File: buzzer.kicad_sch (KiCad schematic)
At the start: 3 parts, among them Q1 BC817

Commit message: Initial component placement
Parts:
- BZ1: footprint (none) -> Buzzer_Beeper:Buzzer_TDK_PS1240P02BT_D12.2mm_H6.5mm
- R11: footprint (none) -> Resistor_SMD:R_0805_2012Metric_Pad1.20x1.40mm_HandSolder
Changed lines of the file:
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@@
 			)
 		)
-		(property "Footprint" ""
+		(property "Footprint" "Resistor_SMD:R_0805_2012Metric_Pad1.20x1.40mm_HandSolder"
 			(at 132.08 103.378 90)
 			(effects
@@
 			)
 		)
-		(property "Footprint" ""
+		(property "Footprint" "Buzzer_Beeper:Buzzer_TDK_PS1240P02BT_D12.2mm_H6.5mm"
 			(at 147.955 90.17 90)
 			(effects

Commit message: Initial layout
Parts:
- added R33: R, Resistor_SMD:R_0805_2012Metric_Pad1.20x1.40mm_HandSolder, symbol Device:R
- BZ1: value Buzzer -> PKMCS0909E48H0-R1; footprint Buzzer_Beeper:Buzzer_TDK_PS1240P02BT_D12.2mm_H6.5mm -> Buzzer_Beeper:Buzzer_Murata_PKLCS1212E
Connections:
- net VCC: now also R33.2
- net at BZ1.2 (-), Q1.3 (C): now also R33.1
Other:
- moved on the sheet: BZ1
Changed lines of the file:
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@@
 	(generator_version "8.0")
 	(paper "A4")
+	(junction
+		(at 144.78 95.25)
+		(diameter 0)
+		(color 0 0 0 0)
+	)
+	(junction
+		(at 144.78 87.63)
+		(diameter 0)
+		(color 0 0 0 0)
+	)
+	(wire
+		(pts
+			(xy 142.24 95.25) (xy 144.78 95.25)
+		)
+		(stroke
+			(width 0)
+			(type default)
+		)
+	)
 	(wire
 		(pts
@@
 	(wire
 		(pts
-			(xy 144.78 90.17) (xy 144.78 88.9)
+			(xy 144.78 88.9) (xy 144.78 87.63)
+		)
+		(stroke
+			(width 0)
+			(type default)
+		)
+	)
+	(wire
+		(pts
+			(xy 142.24 87.63) (xy 144.78 87.63)
 		)
 		(stroke
@@
 	(wire
 		(pts
-			(xy 144.78 95.25) (xy 146.05 95.25)
+			(xy 144.78 87.63) (xy 144.78 82.55)
+		)
+		(stroke
+			(width 0)
+			(type default)
+		)
+	)
+	(wire
+		(pts
+			(xy 144.78 93.98) (xy 148.59 93.98)
+		)
+		(stroke
+			(width 0)
+			(type default)
+		)
+	)
+	(wire
+		(pts
+			(xy 144.78 93.98) (xy 144.78 95.25)
 		)
 		(stroke
@@
 	(wire
 		(pts
-			(xy 144.78 90.17) (xy 146.05 90.17)
+			(xy 144.78 88.9) (xy 148.59 88.9)
 		)
 		(stroke
@@
 				(path "/16b3e55a-9d75-49bf-a6fe-25414eb3d7da/ea853267-6be5-4470-9fb8-da1c0cfa6c51"
 					(reference "#PWR06")
+					(unit 1)
+				)
+			)
+		)
+	)
+	(symbol
+		(lib_id "Device:R")
+		(at 142.24 91.44 180)
+		(unit 1)
+		(exclude_from_sim no)
+		(in_bom yes)
+		(on_board yes)
+		(dnp no)
+		(fields_autoplaced yes)
+		(property "Reference" "R33"
+			(at 144.78 90.1699 0)
+			(effects
+				(font
+					(size 1.27 1.27)
+				)
+				(justify right)
+			)
+		)
+		(property "Value" "R"
+			(at 144.78 92.7099 0)
+			(effects
+				(font
+					(size 1.27 1.27)
+				)
+				(justify right)
+			)
+		)
+		(property "Footprint" "Resistor_SMD:R_0805_2012Metric_Pad1.20x1.40mm_HandSolder"
+			(at 144.018 91.44 90)
+			(effects
+				(font
+					(size 1.27 1.27)
+				)
+				(hide yes)
+			)
+		)
+		(property "Datasheet" "~"
+			(at 142.24 91.44 0)
+			(effects
+				(font
+					(size 1.27 1.27)
+				)
+				(hide yes)
+			)
+		)
+		(property "Description" "Resistor"
+			(at 142.24 91.44 0)
+			(effects
+				(font
+					(size 1.27 1.27)
+				)
+				(hide yes)
+			)
+		)
+		(pin "2"
+		)
+		(pin "1"
+		)
+		(instances
+			(project "LifeCounter"
+				(path "/16b3e55a-9d75-49bf-a6fe-25414eb3d7da/ea853267-6be5-4470-9fb8-da1c0cfa6c51"
+					(reference "R33")
 					(unit 1)
 				)
@@
 	(symbol
 		(lib_id "Device:Buzzer")
-		(at 148.59 92.71 0)
+		(at 151.13 91.44 0)
 		(unit 1)
 		(exclude_from_sim no)
@@
 		(fields_autoplaced yes)
 		(property "Reference" "BZ1"
-			(at 152.4 91.4399 0)
+			(at 154.94 90.1699 0)
 			(effects
 				(font
@@
 			)
 		)
-		(property "Value" "Buzzer"
-			(at 152.4 93.9799 0)
+		(property "Value" "PKMCS0909E48H0-R1"
+			(at 154.94 92.7099 0)
 			(effects
 				(font
@@
 			)
 		)
-		(property "Footprint" "Buzzer_Beeper:Buzzer_TDK_PS1240P02BT_D12.2mm_H6.5mm"
-			(at 147.955 90.17 90)
+		(property "Footprint" "Buzzer_Beeper:Buzzer_Murata_PKLCS1212E"
+			(at 150.495 88.9 90)
 			(effects
 				(font
@@
 		)
 		(property "Datasheet" "~"
-			(at 147.955 90.17 90)
+			(at 150.495 88.9 90)
 			(effects
 				(font
@@
 		)
 		(property "Description" "Buzzer, polarized"
-			(at 148.59 92.71 0)
+			(at 151.13 91.44 0)
 			(effects
 				(font
@@
 	(symbol
 		(lib_id "power:VCC")
-		(at 144.78 88.9 0)
+		(at 144.78 82.55 0)
 		(unit 1)
 		(exclude_from_sim no)
@@
 		(fields_autoplaced yes)
 		(property "Reference" "#PWR03"
-			(at 144.78 92.71 0)
+			(at 144.78 86.36 0)
 			(effects
 				(font
@@
 		)
 		(property "Value" "VCC"
-			(at 144.78 83.82 0)
+			(at 144.78 77.47 0)
 			(effects
 				(font
@@
 		)
 		(property "Footprint" ""
-			(at 144.78 88.9 0)
+			(at 144.78 82.55 0)
 			(effects
 				(font
@@
 		)
 		(property "Datasheet" ""
-			(at 144.78 88.9 0)
+			(at 144.78 82.55 0)
 			(effects
 				(font
@@
 		)
 		(property "Description" "Power symbol creates a global label with name \"VCC\""
-			(at 144.78 88.9 0)
-			(effects
-				(font
+			(at 144.78 82.55 0)
+			(effects
+				(font

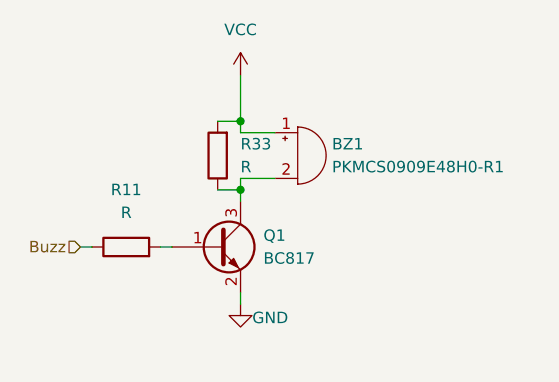
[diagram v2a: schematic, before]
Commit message: Switch transistors to FETs
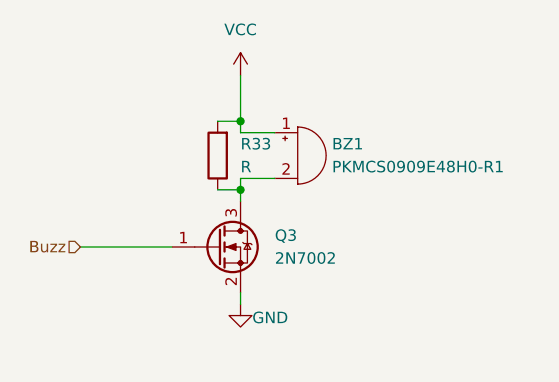
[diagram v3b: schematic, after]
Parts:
- removed Q1: BC817, Package_TO_SOT_SMD:SOT-23, symbol Transistor_BJT:BC817
- removed R11: R, Resistor_SMD:R_0805_2012Metric_Pad1.20x1.40mm_HandSolder, symbol Device:R
- added Q3: 2N7002, Package_TO_SOT_SMD:SOT-23, symbol Transistor_FET:2N7002
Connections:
- net Buzz: now also Q3.1 (G)
- net GND: now also Q3.2 (S)
- net at BZ1.2 (-), R33.1: now also Q3.3 (D)
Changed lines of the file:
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@@
-	(wire
-		(pts
-			(xy 135.89 101.6) (xy 137.16 101.6)
-		)
-		(stroke
-			(width 0)
-			(type default)
-		)
-	)
 	(wire
 		(pts
@@
 	(wire
 		(pts
-			(xy 127 101.6) (xy 128.27 101.6)
+			(xy 127 101.6) (xy 137.16 101.6)
 		)
 		(stroke
@@
 		(shape input)
 		(at 127 101.6 180)
-		(fields_autoplaced yes)
 		(effects
 			(font
@@
 	)
 	(symbol
-		(lib_id "Device:R")
-		(at 132.08 101.6 90)
-		(unit 1)
-		(exclude_from_sim no)
-		(in_bom yes)
-		(on_board yes)
-		(dnp no)
-		(fields_autoplaced yes)
-		(property "Reference" "R11"
-			(at 132.08 95.25 90)
-			(effects
-				(font
-					(size 1.27 1.27)
-				)
-			)
-		)
-		(property "Value" "R"
-			(at 132.08 97.79 90)
-			(effects
-				(font
-					(size 1.27 1.27)
-				)
-			)
-		)
-		(property "Footprint" "Resistor_SMD:R_0805_2012Metric_Pad1.20x1.40mm_HandSolder"
-			(at 132.08 103.378 90)
-			(effects
-				(font
-					(size 1.27 1.27)
-				)
-				(hide yes)
-			)
-		)
-		(property "Datasheet" "~"
-			(at 132.08 101.6 0)
-			(effects
-				(font
-					(size 1.27 1.27)
-				)
-				(hide yes)
-			)
-		)
-		(property "Description" "Resistor"
-			(at 132.08 101.6 0)
-			(effects
-				(font
-					(size 1.27 1.27)
-				)
-				(hide yes)
-			)
-		)
-		(pin "2"
-		)
-		(pin "1"
-		)
-		(instances
-			(project "LifeCounter"
-				(path "/16b3e55a-9d75-49bf-a6fe-25414eb3d7da/ea853267-6be5-4470-9fb8-da1c0cfa6c51"
-					(reference "R11")
-					(unit 1)
-				)
-			)
-		)
-	)
-	(symbol
-		(lib_id "Transistor_BJT:BC817")
+		(lib_id "Transistor_FET:2N7002")
 		(at 142.24 101.6 0)
 		(unit 1)
@@
 		(dnp no)
 		(fields_autoplaced yes)
-		(property "Reference" "Q1"
-			(at 147.32 100.3299 0)
-			(effects
-				(font
-					(size 1.27 1.27)
-				)
-				(justify left)
-			)
-		)
-		(property "Value" "BC817"
-			(at 147.32 102.8699 0)
+		(property "Reference" "Q3"
+			(at 148.59 100.3299 0)
+			(effects
+				(font
+					(size 1.27 1.27)
+				)
+				(justify left)
+			)
+		)
+		(property "Value" "2N7002"
+			(at 148.59 102.8699 0)
 			(effects
 				(font
@@
 			)
 		)
-		(property "Datasheet" "https://www.onsemi.com/pub/Collateral/BC818-D.pdf"
+		(property "Datasheet" "https://www.onsemi.com/pub/Collateral/NDS7002A-D.PDF"
+			(at 147.32 105.41 0)
+			(effects
+				(font
+					(size 1.27 1.27)
+				)
+				(justify left)
+				(hide yes)
+			)
+		)
+		(property "Description" "0.115A Id, 60V Vds, N-Channel MOSFET, SOT-23"
 			(at 142.24 101.6 0)
 			(effects
@@
 					(size 1.27 1.27)
 				)
-				(justify left)
-				(hide yes)
-			)
-		)
-		(property "Description" "0.8A Ic, 45V Vce, NPN Transistor, SOT-23"
-			(at 142.24 101.6 0)
-			(effects
-				(font
-					(size 1.27 1.27)
-				)
 				(hide yes)
 			)
@@
 		)
 		(instances
-			(project "LifeCounter"
+			(project ""
 				(path "/16b3e55a-9d75-49bf-a6fe-25414eb3d7da/ea853267-6be5-4470-9fb8-da1c0cfa6c51"
-					(reference "Q1")
+					(reference "Q3")
 					(unit 1)
 				)

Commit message: KiCAD version update
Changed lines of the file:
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@@
 (kicad_sch
-	(version 20231120)
+	(version 20250114)
 	(generator "eeschema")
-	(generator_version "8.0")
+	(generator_version "9.0")
 	(paper "A4")
 	(junction

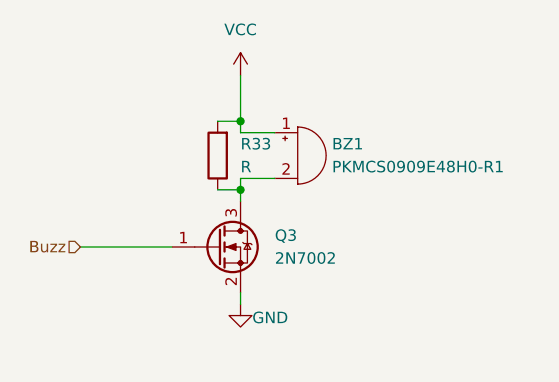
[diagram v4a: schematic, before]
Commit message: Buzzer component value assignment
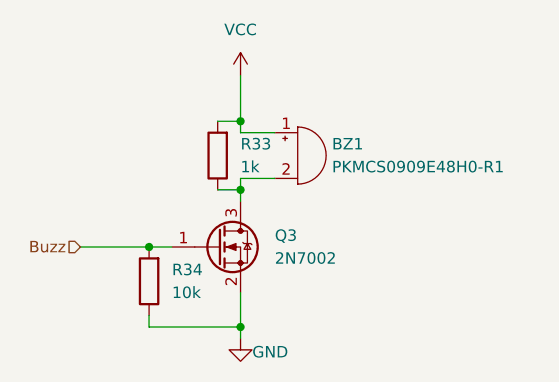
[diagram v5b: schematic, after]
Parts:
- added R34: 10k, Resistor_SMD:R_0805_2012Metric_Pad1.20x1.40mm_HandSolder, symbol Device:R
- R33: value R -> 1k
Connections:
- net Buzz: now also R34.2
- net GND: now also R34.1
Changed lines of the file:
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@@
 	(paper "A4")
+	(junction
+		(at 134.62 101.6)
+		(diameter 0)
+		(color 0 0 0 0)
+	)
 	(junction
 		(at 144.78 95.25)
@@
 		(color 0 0 0 0)
 	)
+	(junction
+		(at 144.78 110.49)
+		(diameter 0)
+		(color 0 0 0 0)
+	)
+	(wire
+		(pts
+			(xy 134.62 109.22) (xy 134.62 110.49)
+		)
+		(stroke
+			(width 0)
+			(type default)
+		)
+	)
 	(wire
 		(pts
@@
 	(wire
 		(pts
+			(xy 134.62 110.49) (xy 144.78 110.49)
+		)
+		(stroke
+			(width 0)
+			(type default)
+		)
+	)
+	(wire
+		(pts
 			(xy 142.24 87.63) (xy 144.78 87.63)
 		)
@@
 	(wire
 		(pts
-			(xy 144.78 106.68) (xy 144.78 107.95)
+			(xy 144.78 106.68) (xy 144.78 110.49)
+		)
+		(stroke
+			(width 0)
+			(type default)
+		)
+	)
+	(wire
+		(pts
+			(xy 134.62 101.6) (xy 137.16 101.6)
 		)
 		(stroke
@@
 	(wire
 		(pts
-			(xy 127 101.6) (xy 137.16 101.6)
+			(xy 127 101.6) (xy 134.62 101.6)
+		)
+		(stroke
+			(width 0)
+			(type default)
+		)
+	)
+	(wire
+		(pts
+			(xy 144.78 111.76) (xy 144.78 110.49)
 		)
 		(stroke
@@
 	(symbol
 		(lib_id "power:GND")
-		(at 144.78 107.95 0)
+		(at 144.78 111.76 0)
 		(unit 1)
 		(exclude_from_sim no)
@@
 		(dnp no)
 		(property "Reference" "#PWR06"
-			(at 144.78 114.3 0)
+			(at 144.78 118.11 0)
 			(effects
 				(font
@@
 		)
 		(property "Value" "GND"
-			(at 148.082 109.474 0)
+			(at 148.082 113.284 0)
 			(effects
 				(font
@@
 		)
 		(property "Footprint" ""
-			(at 144.78 107.95 0)
+			(at 144.78 111.76 0)
 			(effects
 				(font
@@
 		)
 		(property "Datasheet" ""
-			(at 144.78 107.95 0)
+			(at 144.78 111.76 0)
 			(effects
 				(font
@@
 		)
 		(property "Description" "Power symbol creates a global label with name \"GND\" , ground"
-			(at 144.78 107.95 0)
+			(at 144.78 111.76 0)
 			(effects
 				(font
@@
 			)
 		)
-		(property "Value" "R"
+		(property "Value" "1k"
 			(at 144.78 92.7099 0)
 			(effects
@@
 					(unit 1)
 				)
+			)
+		)
+	)
+	(symbol
+		(lib_id "Device:R")
+		(at 134.62 105.41 180)
+		(unit 1)
+		(exclude_from_sim no)
+		(in_bom yes)
+		(on_board yes)
+		(dnp no)
+		(fields_autoplaced yes)
+		(property "Reference" "R34"
+			(at 137.16 104.1399 0)
+			(effects
+				(font
+					(size 1.27 1.27)
+				)
+				(justify right)
+			)
+		)
+		(property "Value" "10k"
+			(at 137.16 106.6799 0)
+			(effects
+				(font
+					(size 1.27 1.27)
+				)
+				(justify right)
+			)
+		)
+		(property "Footprint" "Resistor_SMD:R_0805_2012Metric_Pad1.20x1.40mm_HandSolder"
+			(at 136.398 105.41 90)
+			(effects
+				(font
+					(size 1.27 1.27)
+				)
+				(hide yes)
+			)
+		)
+		(property "Datasheet" "~"
+			(at 134.62 105.41 0)
+			(effects
+				(font
+					(size 1.27 1.27)
+				)
+				(hide yes)
+			)
+		)
+		(property "Description" "Resistor"
+			(at 134.62 105.41 0)
+			(effects
+				(font
+					(size 1.27 1.27)
+				)
+				(hide yes)
+			)
+		)
+		(pin "2"
+		)
+		(pin "1"
+		)
+		(instances
+			(project "LifeCounter"
+				(path "/16b3e55a-9d75-49bf-a6fe-25414eb3d7da/ea853267-6be5-4470-9fb8-da1c0cfa6c51"
+					(reference "R34")
+					(unit 1)
+				)

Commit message: Resolve ERC warnings
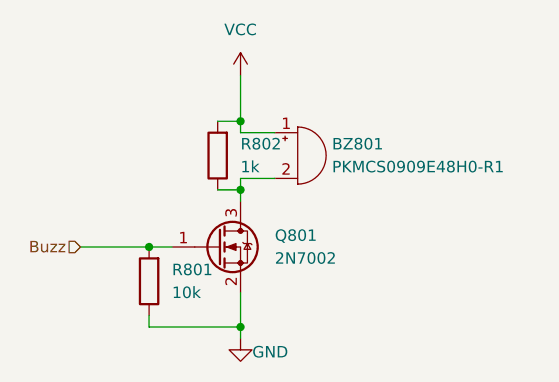
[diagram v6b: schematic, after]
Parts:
- renumbered BZ1 to BZ801, Q3 to Q801, R34 to R801, R33 to R802
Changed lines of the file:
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@@
 		(on_board yes)
 		(dnp no)
-		(property "Reference" "#PWR06"
+		(property "Reference" "#PWR0802"
 			(at 144.78 118.11 0)
 			(effects
@@
 			(project "LifeCounter"
 				(path "/16b3e55a-9d75-49bf-a6fe-25414eb3d7da/ea853267-6be5-4470-9fb8-da1c0cfa6c51"
-					(reference "#PWR06")
+					(reference "#PWR0802")
 					(unit 1)
 				)
@@
 		(dnp no)
 		(fields_autoplaced yes)
-		(property "Reference" "R33"
+		(property "Reference" "R802"
 			(at 144.78 90.1699 0)
 			(effects
@@
 			(project "LifeCounter"
 				(path "/16b3e55a-9d75-49bf-a6fe-25414eb3d7da/ea853267-6be5-4470-9fb8-da1c0cfa6c51"
-					(reference "R33")
+					(reference "R802")
 					(unit 1)
 				)
@@
 		(dnp no)
 		(fields_autoplaced yes)
-		(property "Reference" "R34"
+		(property "Reference" "R801"
 			(at 137.16 104.1399 0)
 			(effects
@@
 			(project "LifeCounter"
 				(path "/16b3e55a-9d75-49bf-a6fe-25414eb3d7da/ea853267-6be5-4470-9fb8-da1c0cfa6c51"
-					(reference "R34")
+					(reference "R801")
 					(unit 1)
 				)
@@
 		(dnp no)
 		(fields_autoplaced yes)
-		(property "Reference" "Q3"
+		(property "Reference" "Q801"
 			(at 148.59 100.3299 0)
 			(effects
@@
 			(project ""
 				(path "/16b3e55a-9d75-49bf-a6fe-25414eb3d7da/ea853267-6be5-4470-9fb8-da1c0cfa6c51"
-					(reference "Q3")
+					(reference "Q801")
 					(unit 1)
 				)
@@
 		(dnp no)
 		(fields_autoplaced yes)
-		(property "Reference" "BZ1"
+		(property "Reference" "BZ801"
 			(at 154.94 90.1699 0)
 			(effects
@@
 			(project "LifeCounter"
 				(path "/16b3e55a-9d75-49bf-a6fe-25414eb3d7da/ea853267-6be5-4470-9fb8-da1c0cfa6c51"
-					(reference "BZ1")
+					(reference "BZ801")
 					(unit 1)
 				)
@@
 		(dnp no)
 		(fields_autoplaced yes)
-		(property "Reference" "#PWR03"
+		(property "Reference" "#PWR0801"
 			(at 144.78 86.36 0)
 			(effects
@@
 			(project "LifeCounter"
 				(path "/16b3e55a-9d75-49bf-a6fe-25414eb3d7da/ea853267-6be5-4470-9fb8-da1c0cfa6c51"
-					(reference "#PWR03")
-					(unit 1)
-				)
+					(reference "#PWR0801")
+					(unit 1)
+				)

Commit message: Footprint selection
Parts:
- BZ801: footprint Buzzer_Beeper:Buzzer_Murata_PKLCS1212E -> Buzzer_Beeper:Buzzer_Murata_PKMCS0909E
- Q801: footprint Package_TO_SOT_SMD:SOT-23 -> Package_TO_SOT_SMD:SOT-23W_Handsoldering
- R801, R802: footprint Resistor_SMD:R_0805_2012Metric_Pad1.20x1.40mm_HandSolder -> Resistor_SMD:R_1206_3216Metric_Pad1.30x1.75mm_HandSolder
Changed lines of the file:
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@@
 			)
 		)
-		(property "Footprint" "Resistor_SMD:R_0805_2012Metric_Pad1.20x1.40mm_HandSolder"
+		(property "Footprint" "Resistor_SMD:R_1206_3216Metric_Pad1.30x1.75mm_HandSolder"
 			(at 144.018 91.44 90)
 			(effects
@@
 			)
 		)
-		(property "Footprint" "Resistor_SMD:R_0805_2012Metric_Pad1.20x1.40mm_HandSolder"
+		(property "Footprint" "Resistor_SMD:R_1206_3216Metric_Pad1.30x1.75mm_HandSolder"
 			(at 136.398 105.41 90)
 			(effects
@@
 			)
 		)
-		(property "Footprint" "Package_TO_SOT_SMD:SOT-23"
+		(property "Footprint" "Package_TO_SOT_SMD:SOT-23W_Handsoldering"
 			(at 147.32 103.505 0)
 			(effects
@@
 			)
 		)
-		(property "Footprint" "Buzzer_Beeper:Buzzer_Murata_PKLCS1212E"
+		(property "Footprint" "Buzzer_Beeper:Buzzer_Murata_PKMCS0909E"
 			(at 150.495 88.9 90)
 			(effects

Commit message: Update component footprint selection
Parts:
- BZ801: footprint Buzzer_Beeper:Buzzer_Murata_PKMCS0909E -> Buzzer_Beeper:Buzzer_12x9.5RM7.6
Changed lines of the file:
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@@
 			)
 		)
-		(property "Footprint" "Buzzer_Beeper:Buzzer_Murata_PKMCS0909E"
+		(property "Footprint" "Buzzer_Beeper:Buzzer_12x9.5RM7.6"
 			(at 150.495 88.9 90)
 			(effects
